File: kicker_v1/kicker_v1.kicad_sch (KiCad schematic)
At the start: 67 parts, among them IC1 SI8620EC-B-IS, IC10 MCP1790, IC3 ADC122S051, IC4 MCP9701A, IC6 MCP6002, IC7 LT3751FE, IC8 FAN3229TMX, Q1 FDS2582, Q2 IKB40N65ES5, Q3 IKB40N65ES5, X1 DF13-12P-1.25V

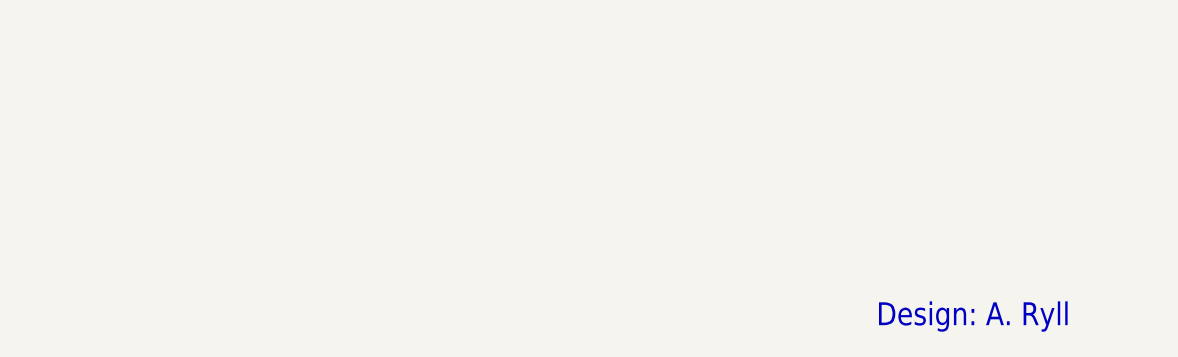
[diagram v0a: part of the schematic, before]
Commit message: File structure enhanced.
Added uniform titleblocks and 3D renders for easier view, file cleanups.
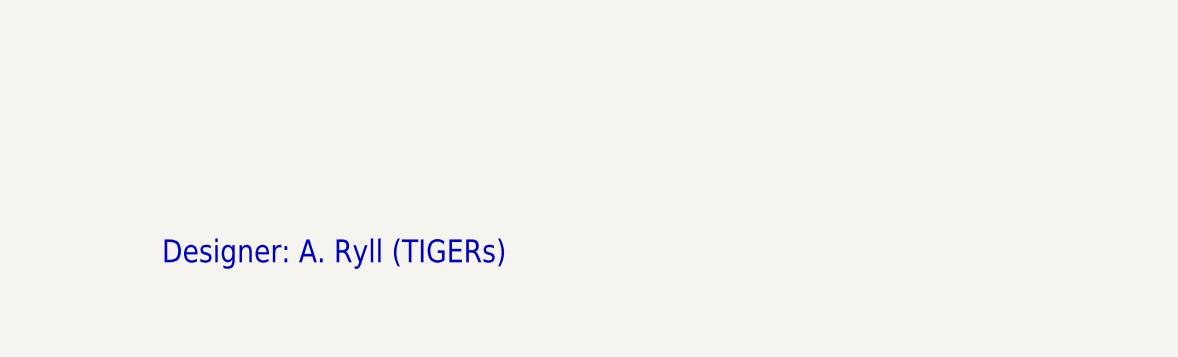
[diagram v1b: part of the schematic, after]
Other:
- note added: "Designer: A. Ryll (TIGERs)"
- note removed: "Design: A. Ryll"
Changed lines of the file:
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@@
 		)
 	)
-	(text "Design: A. Ryll"
+	(text "Designer: A. Ryll (TIGERs)"
 		(exclude_from_sim no)
-		(at 382.905 267.335 0)
+		(at 303.53 260.35 0)
 		(effects
 			(font
